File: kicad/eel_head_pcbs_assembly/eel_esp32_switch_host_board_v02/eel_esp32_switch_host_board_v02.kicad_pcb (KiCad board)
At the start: 2 copper layers, 20.3 x 25 mm, 14 parts, among them J1 Lipo back, J2 motor driver, J3 ELRS RX, J4 Noods front, J5 RGB_DATA, J6 Lipo front, J7 Noods back, Q1 BC817, SW1 SW_Push_DPDT, U1 XIAO-ESP32C3

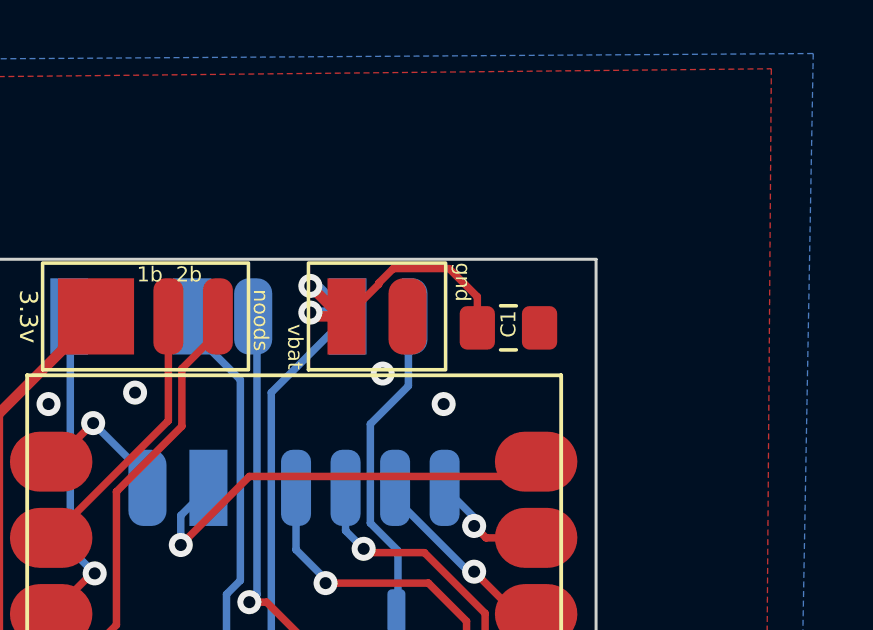
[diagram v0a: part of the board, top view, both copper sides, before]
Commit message: make more room for the pcb holding slot
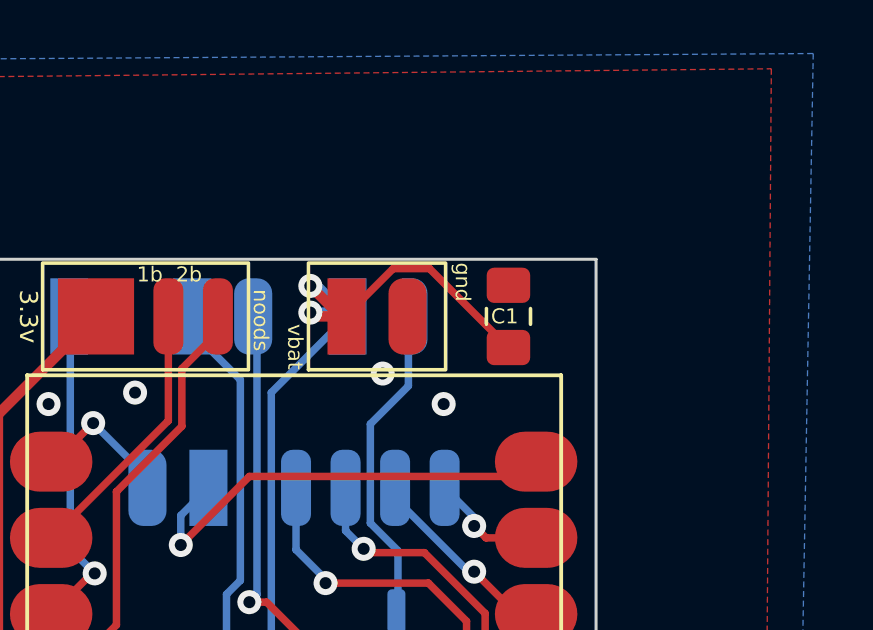
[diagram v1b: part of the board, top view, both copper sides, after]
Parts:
- moved C1 0.38 mm to (102.1, 86.1), turned to 90 degrees
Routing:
- net +BATT: track 32.1 -> 32.8 mm
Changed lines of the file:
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@@
   )
   (footprint "Capacitor_SMD:C_0805_2012Metric_Pad1.18x1.45mm_HandSolder" (layer "F.Cu")
-    (at 102.108 86.487)
+    (at 102.108 86.106 90)
     (descr "Capacitor SMD 0805 (2012 Metric), square (rectangular) end terminal, IPC_7351 nominal with elongated pad for handsoldering. (Body size source: IPC-SM-782 page 76, https://www.pcb-3d.com/wordpress/wp-content/uploads/ipc-sm-782a_amendment_1_and_2.pdf, https://docs.google.com/spreadsheets/d/1BsfQQcO9C6DZCsRaXUlFlo91Tg2WpOkGARC1WS5S8t0/edit?usp=sharing), generated with kicad-footprint-generator")
     (tags "capacitor handsolder")
@@
     (property "Sheetname" "")
     (attr smd)
-    (fp_text reference "C1" (at 0 -0.127 90) (layer "F.SilkS")
+    (fp_text reference "C1" (at 0 -0.127) (layer "F.SilkS")
       (effects (font (size 0.5 0.5) (thickness 0.1)))
     )
-    (fp_text value "C" (at 0 1.68) (layer "F.Fab")
+    (fp_text value "C" (at 0 1.68 90) (layer "F.Fab")
       (effects (font (size 1 1) (thickness 0.15)))
     )
-    (fp_text user "${REFERENCE}" (at 0 0) (layer "F.Fab")
+    (fp_text user "${REFERENCE}" (at 0 0 90) (layer "F.Fab")
       (effects (font (size 0.5 0.5) (thickness 0.08)))
     )
@@
     (fp_line (start 1 -0.625) (end 1 0.625) (layer "F.Fab") (width 0.1))
     (fp_line (start -1 0.625) (end -1 -0.625) (layer "F.Fab") (width 0.1))
-    (pad "1" smd roundrect (at -1.0375 0) (size 1.175 1.45) (layers "F.Cu" "F.Paste" "F.Mask") (roundrect_rratio 0.2127659574)
+    (pad "1" smd roundrect (at -1.0375 0 90) (size 1.175 1.45) (layers "F.Cu" "F.Paste" "F.Mask") (roundrect_rratio 0.2127659574)
       (net 4 "+BATT") (pintype "passive"))
-    (pad "2" smd roundrect (at 1.0375 0) (size 1.175 1.45) (layers "F.Cu" "F.Paste" "F.Mask") (roundrect_rratio 0.2127659574)
+    (pad "2" smd roundrect (at 1.0375 0 90) (size 1.175 1.45) (layers "F.Cu" "F.Paste" "F.Mask") (roundrect_rratio 0.2127659574)
       (net 1 "GND") (pintype "passive"))
     (model "${KICAD6_3DMODEL_DIR}/Capacitor_SMD.3dshapes/C_0805_2012Metric.wrl"
@@
   (segment (start 96.4277 98.9677) (end 99.566 98.9677) (width 0.25) (layer "F.Cu") (net 4))
   (segment (start 96.52 86.106) (end 95.504 85.09) (width 0.35) (layer "F.Cu") (net 4))
-  (segment (start 100.13248 84.51148) (end 98.267273 84.51148) (width 0.25) (layer "F.Cu") (net 4))
+  (segment (start 102.108 87.1435) (end 99.47598 84.51148) (width 0.25) (layer "F.Cu") (net 4))
   (segment (start 96.7118 86.106) (end 95.631 86.106) (width 0.35) (layer "F.Cu") (net 4))
-  (segment (start 98.267273 84.51148) (end 97.78428 84.994473) (width 0.25) (layer "F.Cu") (net 4))
+  (segment (start 98.267273 84.51148) (end 96.7118 86.066953) (width 0.25) (layer "F.Cu") (net 4))
   (segment (start 95.631 86.106) (end 95.504 85.979) (width 0.25) (layer "F.Cu") (net 4))
-  (segment (start 101.0705 85.4495) (end 100.13248 84.51148) (width 0.25) (layer "F.Cu") (net 4))
   (segment (start 96.7118 86.106) (end 96.52 86.106) (width 0.25) (layer "F.Cu") (net 4))
-  (segment (start 97.78428 84.994473) (end 97.78428 85.03352) (width 0.25) (layer "F.Cu") (net 4))
-  (segment (start 97.78428 85.03352) (end 96.7118 86.106) (width 0.25) (layer "F.Cu") (net 4))
-  (segment (start 101.0705 86.487) (end 101.0705 85.4495) (width 0.25) (layer "F.Cu") (net 4))
+  (segment (start 99.47598 84.51148) (end 98.267273 84.51148) (width 0.25) (layer "F.Cu") (net 4))
+  (segment (start 96.7118 86.066953) (end 96.7118 86.106) (width 0.25) (layer "F.Cu") (net 4))
   (via (at 96.139 98.679) (size 0.8) (drill 0.4) (layers "F.Cu" "B.Cu") (net 4))
   (via (at 95.504 85.979) (size 0.8) (drill 0.4) (layers "F.Cu" "B.Cu") (net 4))
